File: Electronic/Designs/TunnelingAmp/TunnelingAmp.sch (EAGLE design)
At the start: 6 parts, among them U1 OPA627AUE4

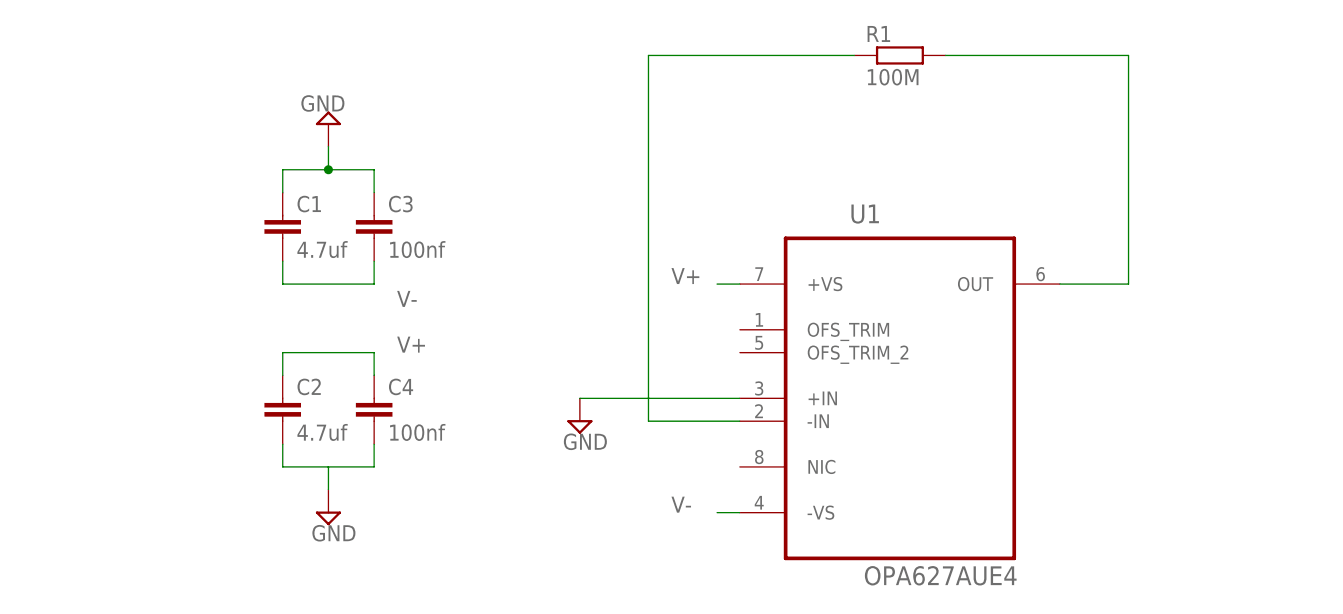
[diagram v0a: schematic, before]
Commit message: Added tunneling current board
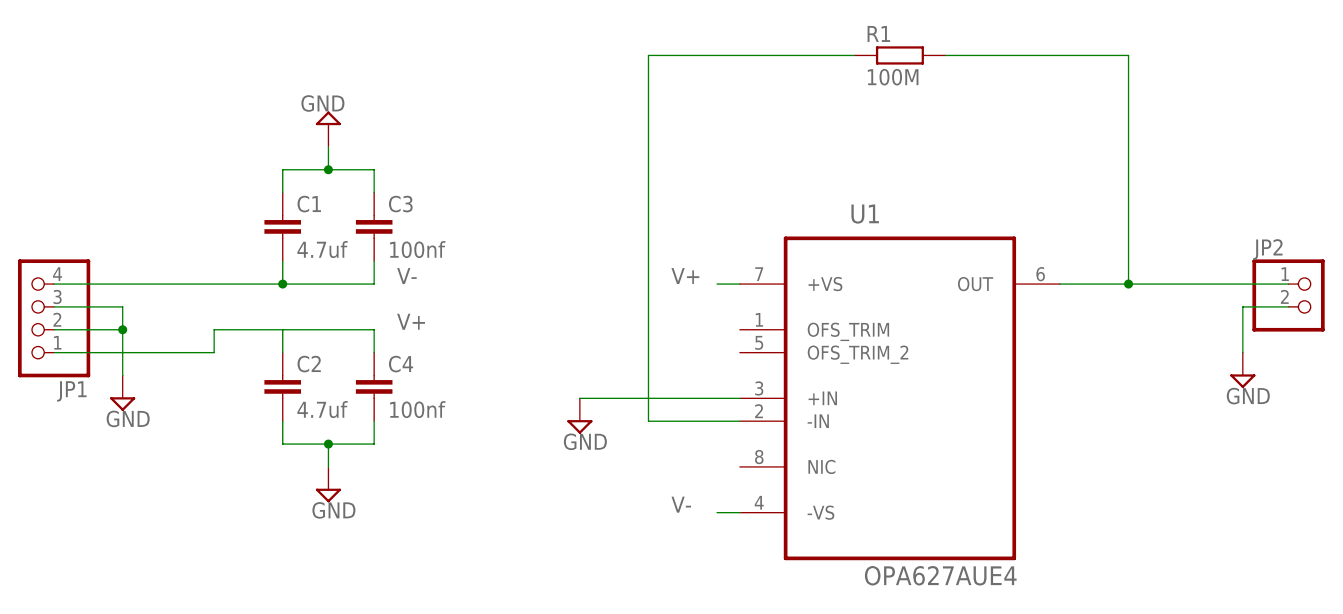
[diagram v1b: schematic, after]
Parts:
- added JP1: (no value), pinhead:PINHD-1X4
- added JP2: (no value), pinhead:PINHD-1X2
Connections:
- net GND: now also JP1.2, JP1.3, JP2.2
- net N$6: now also JP2.1
- net V+: now also JP1.1
- net V-: now also JP1.4
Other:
- moved on the sheet: C2, C4
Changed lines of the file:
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@@
 <part name="R1" library="resistor" deviceset="R-EU_" device="R0805" value="100M"/>
 <part name="SUPPLY3" library="supply2" deviceset="GND" device=""/>
+<part name="JP1" library="pinhead" deviceset="PINHD-1X4" device=""/>
+<part name="SUPPLY4" library="supply2" deviceset="GND" device=""/>
+<part name="JP2" library="pinhead" deviceset="PINHD-1X2" device=""/>
+<part name="SUPPLY5" library="supply2" deviceset="GND" device=""/>
 </parts>
 <sheets>
@@
 <instance part="U1" gate="A" x="45.72" y="38.1"/>
 <instance part="C1" gate="G$1" x="-22.86" y="55.88"/>
-<instance part="C2" gate="G$1" x="-22.86" y="35.56"/>
+<instance part="C2" gate="G$1" x="-22.86" y="38.1"/>
 <instance part="C3" gate="G$1" x="-12.7" y="55.88"/>
-<instance part="C4" gate="G$1" x="-12.7" y="35.56"/>
+<instance part="C4" gate="G$1" x="-12.7" y="38.1"/>
 <instance part="SUPPLY1" gate="GND" x="-17.78" y="66.04" rot="R180"/>
-<instance part="SUPPLY2" gate="GND" x="-17.78" y="22.86"/>
+<instance part="SUPPLY2" gate="GND" x="-17.78" y="25.4"/>
 <instance part="R1" gate="G$1" x="45.72" y="73.66"/>
 <instance part="SUPPLY3" gate="GND" x="10.16" y="33.02"/>
+<instance part="JP1" gate="A" x="-50.8" y="45.72" rot="R180"/>
+<instance part="SUPPLY4" gate="GND" x="-40.64" y="35.56"/>
+<instance part="JP2" gate="G$1" x="91.44" y="45.72"/>
+<instance part="SUPPLY5" gate="GND" x="83.82" y="38.1"/>
 </instances>
 <busses>
@@
 <segment>
 <pinref part="C4" gate="G$1" pin="1"/>
-<wire x1="-12.7" y1="38.1" x2="-12.7" y2="40.64" width="0.1524" layer="91"/>
+<wire x1="-12.7" y1="40.64" x2="-12.7" y2="43.18" width="0.1524" layer="91"/>
 <pinref part="C2" gate="G$1" pin="1"/>
-<wire x1="-12.7" y1="40.64" x2="-22.86" y2="40.64" width="0.1524" layer="91"/>
-<wire x1="-22.86" y1="40.64" x2="-22.86" y2="38.1" width="0.1524" layer="91"/>
-<label x="-10.16" y="40.64" size="1.778" layer="95"/>
+<wire x1="-12.7" y1="43.18" x2="-22.86" y2="43.18" width="0.1524" layer="91"/>
+<label x="-10.16" y="43.18" size="1.778" layer="95"/>
+<pinref part="JP1" gate="A" pin="1"/>
+<wire x1="-48.26" y1="40.64" x2="-30.48" y2="40.64" width="0.1524" layer="91"/>
+<wire x1="-30.48" y1="40.64" x2="-30.48" y2="43.18" width="0.1524" layer="91"/>
+<wire x1="-30.48" y1="43.18" x2="-22.86" y2="43.18" width="0.1524" layer="91"/>
+<wire x1="-22.86" y1="43.18" x2="-22.86" y2="40.64" width="0.1524" layer="91"/>
 </segment>
 </net>
@@
 <pinref part="C1" gate="G$1" pin="2"/>
 <wire x1="-22.86" y1="48.26" x2="-22.86" y2="50.8" width="0.1524" layer="91"/>
-<label x="-10.16" y="45.72" size="1.778" layer="95"/>
+<label x="-10.16" y="48.26" size="1.778" layer="95"/>
+<pinref part="JP1" gate="A" pin="4"/>
+<wire x1="-22.86" y1="48.26" x2="-48.26" y2="48.26" width="0.1524" layer="91"/>
+<junction x="-22.86" y="48.26"/>
 </segment>
 </net>
@@
 <segment>
 <pinref part="C2" gate="G$1" pin="2"/>
-<wire x1="-22.86" y1="30.48" x2="-22.86" y2="27.94" width="0.1524" layer="91"/>
-<wire x1="-22.86" y1="27.94" x2="-17.78" y2="27.94" width="0.1524" layer="91"/>
+<wire x1="-22.86" y1="33.02" x2="-22.86" y2="30.48" width="0.1524" layer="91"/>
+<wire x1="-22.86" y1="30.48" x2="-17.78" y2="30.48" width="0.1524" layer="91"/>
 <pinref part="C4" gate="G$1" pin="2"/>
-<wire x1="-17.78" y1="27.94" x2="-12.7" y2="27.94" width="0.1524" layer="91"/>
-<wire x1="-12.7" y1="27.94" x2="-12.7" y2="30.48" width="0.1524" layer="91"/>
+<wire x1="-17.78" y1="30.48" x2="-12.7" y2="30.48" width="0.1524" layer="91"/>
+<wire x1="-12.7" y1="30.48" x2="-12.7" y2="33.02" width="0.1524" layer="91"/>
 <pinref part="SUPPLY2" gate="GND" pin="GND"/>
-<wire x1="-17.78" y1="25.4" x2="-17.78" y2="27.94" width="0.1524" layer="91"/>
+<wire x1="-17.78" y1="27.94" x2="-17.78" y2="30.48" width="0.1524" layer="91"/>
+<junction x="-17.78" y="30.48"/>
 </segment>
 <segment>
@@
 <pinref part="SUPPLY3" gate="GND" pin="GND"/>
 <wire x1="27.94" y1="35.56" x2="10.16" y2="35.56" width="0.1524" layer="91"/>
+</segment>
+<segment>
+<pinref part="JP1" gate="A" pin="3"/>
+<wire x1="-48.26" y1="45.72" x2="-40.64" y2="45.72" width="0.1524" layer="91"/>
+<pinref part="SUPPLY4" gate="GND" pin="GND"/>
+<wire x1="-40.64" y1="45.72" x2="-40.64" y2="43.18" width="0.1524" layer="91"/>
+<junction x="-40.64" y="43.18"/>
+<wire x1="-40.64" y1="43.18" x2="-40.64" y2="38.1" width="0.1524" layer="91"/>
+<pinref part="JP1" gate="A" pin="2"/>
+<wire x1="-48.26" y1="43.18" x2="-40.64" y2="43.18" width="0.1524" layer="91"/>
+</segment>
+<segment>
+<pinref part="JP2" gate="G$1" pin="2"/>
+<pinref part="SUPPLY5" gate="GND" pin="GND"/>
+<wire x1="88.9" y1="45.72" x2="83.82" y2="45.72" width="0.1524" layer="91"/>
+<wire x1="83.82" y1="45.72" x2="83.82" y2="40.64" width="0.1524" layer="91"/>
 </segment>
 </net>
@@
 <pinref part="R1" gate="G$1" pin="2"/>
 <wire x1="71.12" y1="73.66" x2="50.8" y2="73.66" width="0.1524" layer="91"/>
+<pinref part="JP2" gate="G$1" pin="1"/>
+<wire x1="88.9" y1="48.26" x2="71.12" y2="48.26" width="0.1524" layer="91"/>
+<junction x="71.12" y="48.26"/>
 </segment>
 </net>

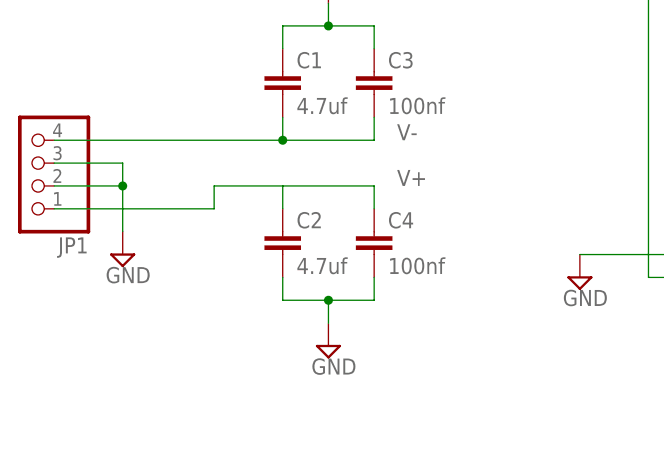
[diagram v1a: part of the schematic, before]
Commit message: Added guard ring to tunneling current amp
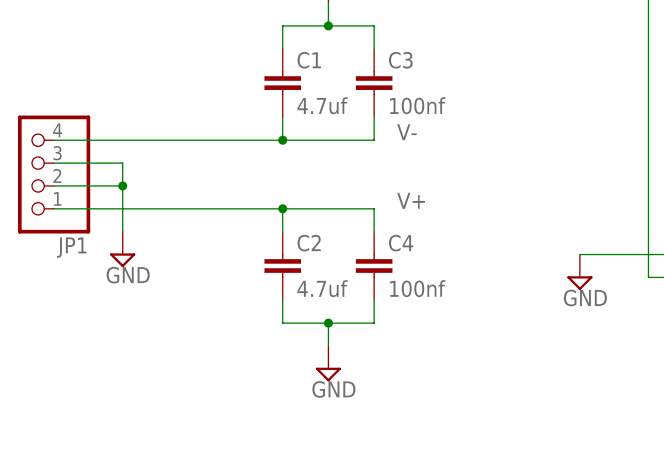
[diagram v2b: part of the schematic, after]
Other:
- moved on the sheet: C2, C4
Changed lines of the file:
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@@
 <instance part="U1" gate="A" x="45.72" y="38.1"/>
 <instance part="C1" gate="G$1" x="-22.86" y="55.88"/>
-<instance part="C2" gate="G$1" x="-22.86" y="38.1"/>
+<instance part="C2" gate="G$1" x="-22.86" y="35.56"/>
 <instance part="C3" gate="G$1" x="-12.7" y="55.88"/>
-<instance part="C4" gate="G$1" x="-12.7" y="38.1"/>
+<instance part="C4" gate="G$1" x="-12.7" y="35.56"/>
 <instance part="SUPPLY1" gate="GND" x="-17.78" y="66.04" rot="R180"/>
-<instance part="SUPPLY2" gate="GND" x="-17.78" y="25.4"/>
+<instance part="SUPPLY2" gate="GND" x="-17.78" y="22.86"/>
 <instance part="R1" gate="G$1" x="45.72" y="73.66"/>
 <instance part="SUPPLY3" gate="GND" x="10.16" y="33.02"/>
@@
 <segment>
 <pinref part="C4" gate="G$1" pin="1"/>
-<wire x1="-12.7" y1="40.64" x2="-12.7" y2="43.18" width="0.1524" layer="91"/>
+<wire x1="-12.7" y1="38.1" x2="-12.7" y2="40.64" width="0.1524" layer="91"/>
 <pinref part="C2" gate="G$1" pin="1"/>
-<wire x1="-12.7" y1="43.18" x2="-22.86" y2="43.18" width="0.1524" layer="91"/>
-<label x="-10.16" y="43.18" size="1.778" layer="95"/>
+<wire x1="-12.7" y1="40.64" x2="-22.86" y2="40.64" width="0.1524" layer="91"/>
+<label x="-10.16" y="40.64" size="1.778" layer="95"/>
 <pinref part="JP1" gate="A" pin="1"/>
-<wire x1="-48.26" y1="40.64" x2="-30.48" y2="40.64" width="0.1524" layer="91"/>
-<wire x1="-30.48" y1="40.64" x2="-30.48" y2="43.18" width="0.1524" layer="91"/>
-<wire x1="-30.48" y1="43.18" x2="-22.86" y2="43.18" width="0.1524" layer="91"/>
-<wire x1="-22.86" y1="43.18" x2="-22.86" y2="40.64" width="0.1524" layer="91"/>
+<wire x1="-48.26" y1="40.64" x2="-22.86" y2="40.64" width="0.1524" layer="91"/>
+<wire x1="-22.86" y1="40.64" x2="-22.86" y2="38.1" width="0.1524" layer="91"/>
+<junction x="-22.86" y="40.64"/>
 </segment>
 </net>
@@
 <segment>
 <pinref part="C2" gate="G$1" pin="2"/>
-<wire x1="-22.86" y1="33.02" x2="-22.86" y2="30.48" width="0.1524" layer="91"/>
-<wire x1="-22.86" y1="30.48" x2="-17.78" y2="30.48" width="0.1524" layer="91"/>
+<wire x1="-22.86" y1="30.48" x2="-22.86" y2="27.94" width="0.1524" layer="91"/>
+<wire x1="-22.86" y1="27.94" x2="-17.78" y2="27.94" width="0.1524" layer="91"/>
 <pinref part="C4" gate="G$1" pin="2"/>
-<wire x1="-17.78" y1="30.48" x2="-12.7" y2="30.48" width="0.1524" layer="91"/>
-<wire x1="-12.7" y1="30.48" x2="-12.7" y2="33.02" width="0.1524" layer="91"/>
+<wire x1="-17.78" y1="27.94" x2="-12.7" y2="27.94" width="0.1524" layer="91"/>
+<wire x1="-12.7" y1="27.94" x2="-12.7" y2="30.48" width="0.1524" layer="91"/>
 <pinref part="SUPPLY2" gate="GND" pin="GND"/>
-<wire x1="-17.78" y1="27.94" x2="-17.78" y2="30.48" width="0.1524" layer="91"/>
-<junction x="-17.78" y="30.48"/>
+<wire x1="-17.78" y1="25.4" x2="-17.78" y2="27.94" width="0.1524" layer="91"/>
+<junction x="-17.78" y="27.94"/>
 </segment>
 <segment>

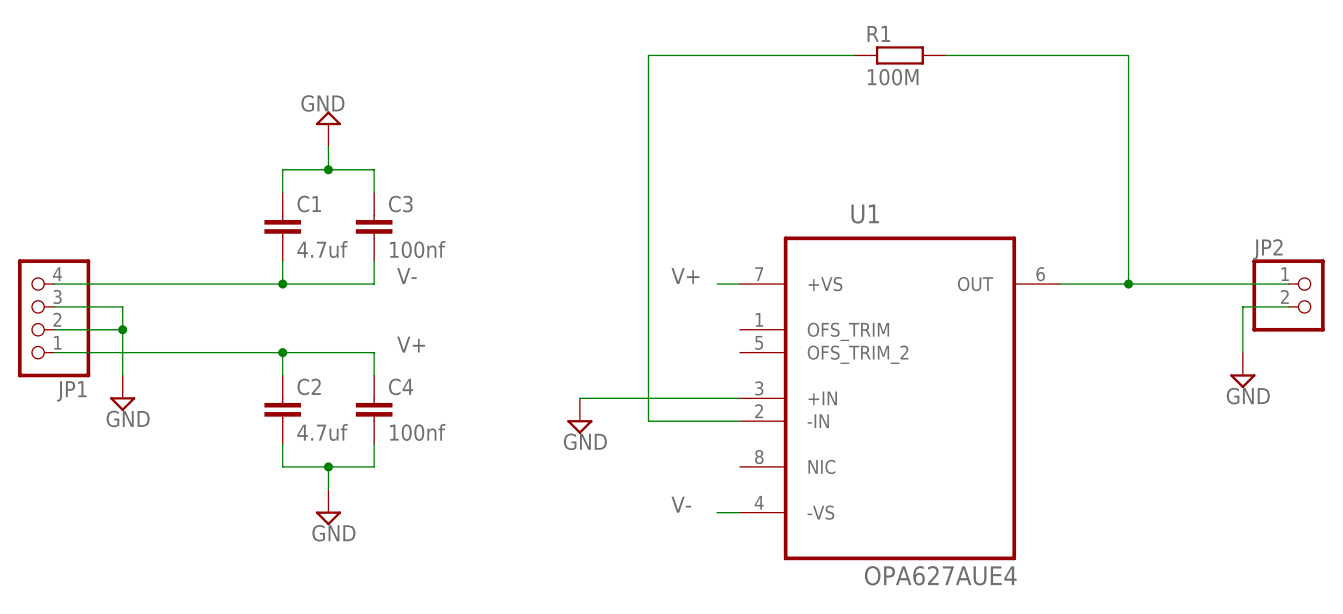
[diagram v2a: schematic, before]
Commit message: Added to tunneling amp
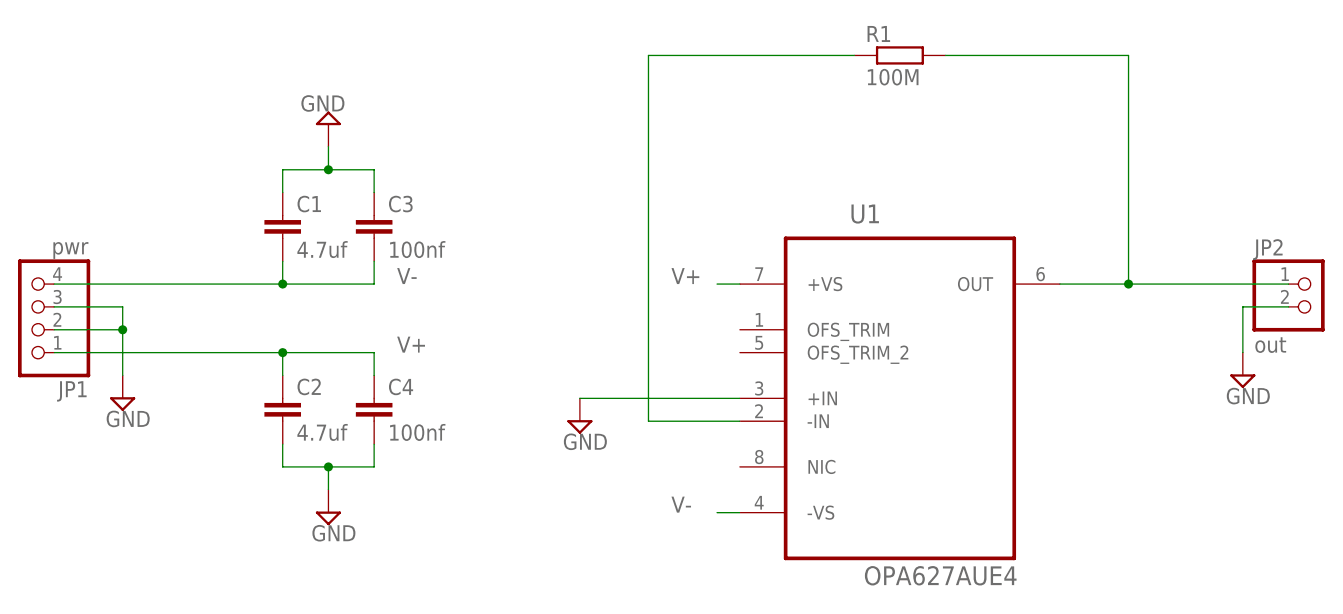
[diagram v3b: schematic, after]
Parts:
- JP1: value (none) -> pwr
- JP2: value (none) -> out
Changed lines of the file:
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@@
 <part name="R1" library="resistor" deviceset="R-EU_" device="R0805" value="100M"/>
 <part name="SUPPLY3" library="supply2" deviceset="GND" device=""/>
-<part name="JP1" library="pinhead" deviceset="PINHD-1X4" device=""/>
+<part name="JP1" library="pinhead" deviceset="PINHD-1X4" device="" value="pwr"/>
 <part name="SUPPLY4" library="supply2" deviceset="GND" device=""/>
-<part name="JP2" library="pinhead" deviceset="PINHD-1X2" device=""/>
+<part name="JP2" library="pinhead" deviceset="PINHD-1X2" device="" value="out"/>
 <part name="SUPPLY5" library="supply2" deviceset="GND" device=""/>
 </parts>
